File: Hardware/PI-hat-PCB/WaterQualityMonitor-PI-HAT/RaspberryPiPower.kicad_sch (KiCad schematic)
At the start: 27 parts

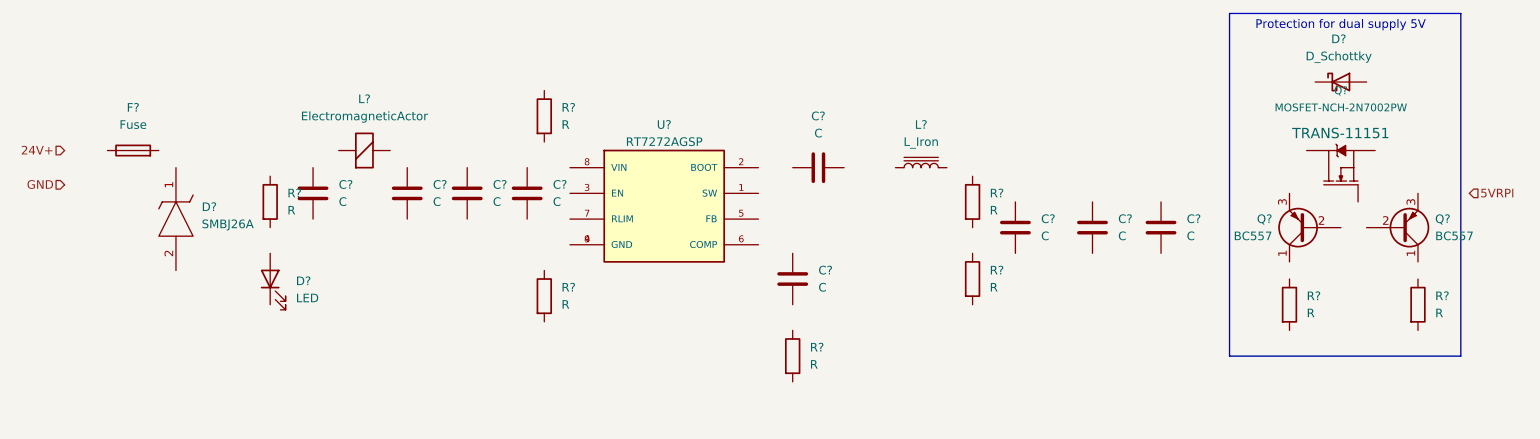
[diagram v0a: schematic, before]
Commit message: Finished powermanagementsystem
added RPI powersupply
added 5V and 3.3V power supply
changed some components (errors)
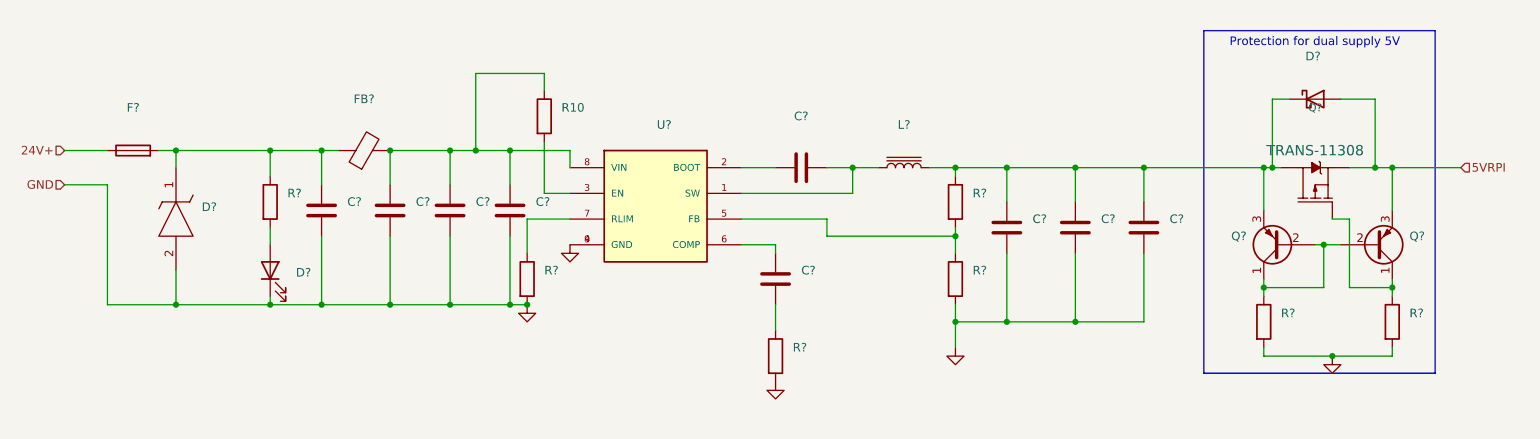
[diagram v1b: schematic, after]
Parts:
- removed C? (x4): C, symbol Device:C
- removed L?: ElectromagneticActor, symbol Device:ElectromagneticActor
- removed Q?: MOSFET-NCH-2N7002PW, SOT323, symbol SparkFun-DiscreteSemi:MOSFET-NCH-2N7002PW
- added C? (x4): (no value), symbol Device:C
- added FB?: (no value), symbol Device:FerriteBead
- added Q?: (no value), symbol SparkFun-DiscreteSemi:MOSFET_PCH-DMG2307L
- C? (x5): value C -> (none)
- D?: value D_Schottky -> (none)
- D?: value SMBJ26A -> (none); footprint DIOM5436X244N -> (none)
- D?: value LED -> (none)
- F?: value Fuse -> (none)
- L?: value L_Iron -> (none)
- Q? (x2): value BC557 -> (none); footprint Package_TO_SOT_THT:TO-92_Inline -> (none)
- R10: renamed from R?; value R -> (none)
- R? (x7): value R -> (none)
- U?: value RT7272AGSP -> (none); footprint SOIC127P599X175-9N -> (none)
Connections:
- net 24V+: now also F?.1
- net 5VRPI: now also D?.2 (A), Q?.3 (E), Q?.2 (S)
- net GND: now also C?.1, C?.1, C?.2, D?.1 (K), D?.2, R?.2, R?.2, R?.2, R?.2, R?.2, U?.4 (GND), U?.9 (GND), C?.1, C?.2, C?.2, C?.2
- net at R?.1: now also C?.1, D?.1, F?.2, FB?.1
- net at R?.2: now also D?.2 (A)
- net at R?.1: now also Q?.1 (C), Q?.1 (G)
- net at Q?.1 (C): now also Q?.2 (B), Q?.2 (B), R?.1
- net at Q?.3 (E): now also C?.2, C?.2, D?.1 (K), L?.2, R?.1, C?.2, Q?.3 (D)
- net at R10.1: now also U?.8 (VIN), C?.1, C?.1, C?.1, FB?.2
- net at R10.2: now also U?.3 (EN)
- net at R?.1: now also C?.1
- net at R?.1: now also U?.7 (RLIM)
- net at U?.1 (SW): now also C?.2, L?.1
- net at U?.2 (BOOT): now also C?.1
- net at U?.5 (FB): now also R?.1, R?.2
- net at U?.6 (COMP): now also C?.2
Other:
- moved on the sheet: C?, D?, L?, Q?, R?, U?

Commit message: started heating and cooling design
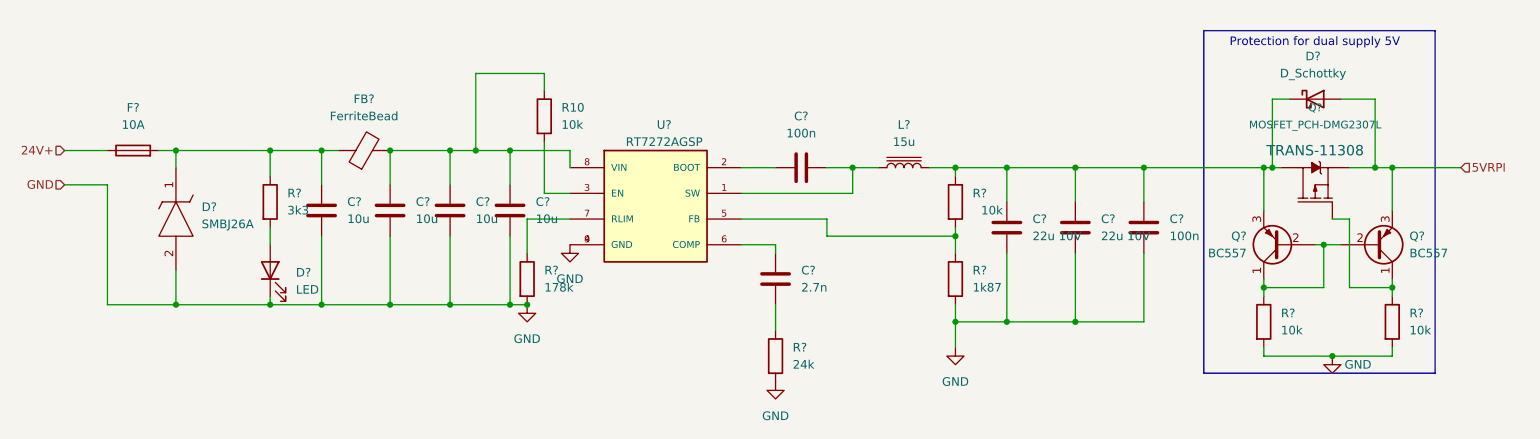
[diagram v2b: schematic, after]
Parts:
- C? (x4): value (none) -> 10u
- C? (x2): value (none) -> 22u 10V
- C? (x2): value (none) -> 100n
- C?: value (none) -> 2.7n
- D?: value (none) -> D_Schottky
- D?: value (none) -> SMBJ26A; footprint (none) -> DIOM5436X244N
- D?: value (none) -> LED
- F?: value (none) -> 10A
- FB?: value (none) -> FerriteBead
- L?: value (none) -> 15u
- Q?: value (none) -> MOSFET_PCH-DMG2307L; footprint (none) -> SOT23-3
- Q? (x2): value (none) -> BC557; footprint (none) -> Package_TO_SOT_THT:TO-92_Inline
- R10, R? (x3): value (none) -> 10k
- R?: value (none) -> 3k3
- R?: value (none) -> 24k
- R?: value (none) -> 178k
- R?: value (none) -> 1k87
- U?: value (none) -> RT7272AGSP; footprint (none) -> SOIC127P599X175-9N
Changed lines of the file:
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@@
       (effects (font (size 1.143 1.143)))
     )
-    (property "Value" "" (id 1) (at 232.41 87.63 90)
+    (property "Value" "MOSFET_PCH-DMG2307L" (id 1) (at 232.41 87.63 90)
       (effects (font (size 1.143 1.143)))
     )
-    (property "Footprint" "" (id 2) (at 226.06 96.52 0)
+    (property "Footprint" "SOT23-3" (id 2) (at 226.06 96.52 0)
       (effects (font (size 0.508 0.508)) hide)
     )
@@
       (effects (font (size 1.27 1.27)) (justify left))
     )
-    (property "Value" "" (id 1) (at 80.01 100.3299 0)
+    (property "Value" "3k3" (id 1) (at 80.01 100.3299 0)
       (effects (font (size 1.27 1.27)) (justify left))
     )
@@
       (effects (font (size 1.27 1.27)) (justify left))
     )
-    (property "Value" "" (id 1) (at 246.38 118.1099 0)
+    (property "Value" "10k" (id 1) (at 246.38 118.1099 0)
       (effects (font (size 1.27 1.27)) (justify left))
     )
@@
       (effects (font (size 1.27 1.27)) (justify left))
     )
-    (property "Value" "" (id 1) (at 222.25 106.6799 0)
-      (effects (font (size 1.27 1.27)) (justify left))
-    )
-    (property "Footprint" "" (id 2) (at 222.25 103.505 0)
+    (property "Value" "BC557" (id 1) (at 222.25 106.6799 0)
+      (effects (font (size 1.27 1.27)) (justify left))
+    )
+    (property "Footprint" "Package_TO_SOT_THT:TO-92_Inline" (id 2) (at 222.25 103.505 0)
       (effects (font (size 1.27 1.27) italic) (justify left) hide)
     )
@@
       (effects (font (size 1.27 1.27)) (justify left))
     )
-    (property "Value" "" (id 1) (at 120.65 87.6299 0)
+    (property "Value" "10k" (id 1) (at 120.65 87.6299 0)
       (effects (font (size 1.27 1.27)) (justify left))
     )
@@
       (effects (font (size 1.27 1.27)) (justify left))
     )
-    (property "Value" "" (id 1) (at 154.94 123.1899 0)
+    (property "Value" "24k" (id 1) (at 154.94 123.1899 0)
       (effects (font (size 1.27 1.27)) (justify left))
     )
@@
       (effects (font (size 1.27 1.27)) (justify left))
     )
-    (property "Value" "" (id 1) (at 118.11 111.7599 0)
+    (property "Value" "178k" (id 1) (at 118.11 111.7599 0)
       (effects (font (size 1.27 1.27)) (justify left))
     )
@@
       (effects (font (size 1.27 1.27)) (justify left))
     )
-    (property "Value" "" (id 1) (at 227.33 118.1099 0)
+    (property "Value" "10k" (id 1) (at 227.33 118.1099 0)
       (effects (font (size 1.27 1.27)) (justify left))
     )
@@
       (effects (font (size 1.27 1.27)) (justify left))
     )
-    (property "Value" "" (id 1) (at 88.9 101.5999 0)
+    (property "Value" "10u" (id 1) (at 88.9 101.5999 0)
       (effects (font (size 1.27 1.27)) (justify left))
     )
@@
       (effects (font (size 1.27 1.27)) (justify right))
     )
-    (property "Value" "" (id 1) (at 190.5 104.1399 0)
+    (property "Value" "22u 10V" (id 1) (at 190.5 104.1399 0)
       (effects (font (size 1.27 1.27)) (justify right))
     )
@@
       (effects (font (size 1.27 1.27)) (justify left))
     )
-    (property "Value" "" (id 1) (at 99.06 101.5999 0)
+    (property "Value" "10u" (id 1) (at 99.06 101.5999 0)
       (effects (font (size 1.27 1.27)) (justify left))
     )
@@
       (effects (font (size 1.27 1.27)) (justify left))
     )
-    (property "Value" "" (id 1) (at 246.38 106.6799 0)
-      (effects (font (size 1.27 1.27)) (justify left))
-    )
-    (property "Footprint" "" (id 2) (at 246.38 103.505 0)
+    (property "Value" "BC557" (id 1) (at 246.38 106.6799 0)
+      (effects (font (size 1.27 1.27)) (justify left))
+    )
+    (property "Footprint" "Package_TO_SOT_THT:TO-92_Inline" (id 2) (at 246.38 103.505 0)
       (effects (font (size 1.27 1.27) italic) (justify left) hide)
     )
@@
       (effects (font (size 1.27 1.27)) (justify right))
     )
-    (property "Value" "" (id 1) (at 210.82 104.1399 0)
+    (property "Value" "100n" (id 1) (at 210.82 104.1399 0)
       (effects (font (size 1.27 1.27)) (justify right))
     )
@@
       (effects (font (size 1.27 1.27)) (justify left))
     )
-    (property "Value" "" (id 1) (at 107.95 101.5999 0)
+    (property "Value" "10u" (id 1) (at 107.95 101.5999 0)
       (effects (font (size 1.27 1.27)) (justify left))
     )
@@
     (in_bom yes) (on_board yes) (fields_autoplaced)
     (property "Reference" "D?" (id 0) (at 232.0925 77.47 0))
-    (property "Value" "" (id 1) (at 232.0925 80.01 0))
+    (property "Value" "D_Schottky" (id 1) (at 232.0925 80.01 0))
     (property "Footprint" "" (id 2) (at 232.41 83.82 0)
       (effects (font (size 1.27 1.27)) hide)
@@
       (effects (font (size 1.27 1.27)) hide)
     )
-    (property "Value" "" (id 1) (at 238.76 123.19 0))
+    (property "Value" "GND" (id 1) (at 238.76 123.19 0))
     (property "Footprint" "" (id 2) (at 234.95 121.92 0)
       (effects (font (size 1.27 1.27)) hide)
@@
     (in_bom yes) (on_board yes) (fields_autoplaced)
     (property "Reference" "FB?" (id 0) (at 91.3892 83.82 90))
-    (property "Value" "" (id 1) (at 91.3892 86.36 90))
+    (property "Value" "FerriteBead" (id 1) (at 91.3892 86.36 90))
     (property "Footprint" "" (id 2) (at 91.44 93.218 90)
       (effects (font (size 1.27 1.27)) hide)
@@
       (effects (font (size 1.27 1.27)) (justify left))
     )
-    (property "Value" "" (id 1) (at 67.31 102.3619 90)
-      (effects (font (size 1.27 1.27)) (justify left))
-    )
-    (property "Footprint" "" (id 2) (at 67.31 104.14 0)
+    (property "Value" "SMBJ26A" (id 1) (at 67.31 102.3619 90)
+      (effects (font (size 1.27 1.27)) (justify left))
+    )
+    (property "Footprint" "DIOM5436X244N" (id 2) (at 67.31 104.14 0)
       (effects (font (size 1.27 1.27)) (justify left bottom) hide)
     )
@@
     (in_bom yes) (on_board yes) (fields_autoplaced)
     (property "Reference" "U?" (id 0) (at 135.89 87.63 0))
-    (property "Value" "" (id 1) (at 135.89 90.17 0))
-    (property "Footprint" "" (id 2) (at 127 110.49 0)
+    (property "Value" "RT7272AGSP" (id 1) (at 135.89 90.17 0))
+    (property "Footprint" "SOIC127P599X175-9N" (id 2) (at 127 110.49 0)
       (effects (font (size 1.27 1.27)) (justify left bottom) hide)
     )
@@
       (effects (font (size 1.27 1.27)) (justify right))
     )
-    (property "Value" "" (id 1) (at 81.28 112.0774 90)
+    (property "Value" "LED" (id 1) (at 81.28 112.0774 90)
       (effects (font (size 1.27 1.27)) (justify right))
     )
@@
       (effects (font (size 1.27 1.27)) hide)
     )
-    (property "Value" "" (id 1) (at 179.07 125.73 0))
+    (property "Value" "GND" (id 1) (at 179.07 125.73 0))
     (property "Footprint" "" (id 2) (at 179.07 120.65 0)
       (effects (font (size 1.27 1.27)) hide)
@@
       (effects (font (size 1.27 1.27)) hide)
     )
-    (property "Value" "" (id 1) (at 121.92 110.49 0))
+    (property "Value" "GND" (id 1) (at 121.92 110.49 0))
     (property "Footprint" "" (id 2) (at 121.92 105.41 0)
       (effects (font (size 1.27 1.27)) hide)
@@
       (effects (font (size 1.27 1.27)) (justify right))
     )
-    (property "Value" "" (id 1) (at 156.21 111.7599 0)
+    (property "Value" "2.7n" (id 1) (at 156.21 111.7599 0)
       (effects (font (size 1.27 1.27)) (justify right))
     )
@@
       (effects (font (size 1.27 1.27)) (justify right))
     )
-    (property "Value" "" (id 1) (at 200.66 104.1399 0)
+    (property "Value" "22u 10V" (id 1) (at 200.66 104.1399 0)
       (effects (font (size 1.27 1.27)) (justify right))
     )
@@
       (effects (font (size 1.27 1.27)) (justify left))
     )
-    (property "Value" "" (id 1) (at 182.88 100.3299 0)
+    (property "Value" "10k" (id 1) (at 182.88 100.3299 0)
       (effects (font (size 1.27 1.27)) (justify left))
     )
@@
       (effects (font (size 1.27 1.27)) (justify left))
     )
-    (property "Value" "" (id 1) (at 181.61 111.7599 0)
+    (property "Value" "1k87" (id 1) (at 181.61 111.7599 0)
       (effects (font (size 1.27 1.27)) (justify left))
     )
@@
       (effects (font (size 1.27 1.27)) hide)
     )
-    (property "Value" "" (id 1) (at 152.4 130.81 0))
+    (property "Value" "GND" (id 1) (at 152.4 130.81 0))
     (property "Footprint" "" (id 2) (at 152.4 125.73 0)
       (effects (font (size 1.27 1.27)) hide)
@@
     (in_bom yes) (on_board yes) (fields_autoplaced)
     (property "Reference" "C?" (id 0) (at 156.21 86.36 90))
-    (property "Value" "" (id 1) (at 156.21 88.9 90))
+    (property "Value" "100n" (id 1) (at 156.21 88.9 90))
     (property "Footprint" "" (id 2) (at 160.02 93.0148 0)
       (effects (font (size 1.27 1.27)) hide)
@@
       (effects (font (size 1.27 1.27)) (justify left))
     )
-    (property "Value" "" (id 1) (at 116.84 101.5999 0)
+    (property "Value" "10u" (id 1) (at 116.84 101.5999 0)
       (effects (font (size 1.27 1.27)) (justify left))
     )
@@
     (in_bom yes) (on_board yes) (fields_autoplaced)
     (property "Reference" "L?" (id 0) (at 171.45 87.63 90))
-    (property "Value" "" (id 1) (at 171.45 90.17 90))
+    (property "Value" "15u" (id 1) (at 171.45 90.17 90))
     (property "Footprint" "" (id 2) (at 171.45 93.98 0)
       (effects (font (size 1.27 1.27)) hide)
@@
       (effects (font (size 1.27 1.27)) hide)
     )
-    (property "Value" "" (id 1) (at 115.57 119.38 0))
+    (property "Value" "GND" (id 1) (at 115.57 119.38 0))
     (property "Footprint" "" (id 2) (at 115.57 114.3 0)
       (effects (font (size 1.27 1.27)) hide)
@@
     (in_bom yes) (on_board yes) (fields_autoplaced)
     (property "Reference" "F?" (id 0) (at 57.15 85.09 90))
-    (property "Value" "" (id 1) (at 57.15 87.63 90))
+    (property "Value" "10A" (id 1) (at 57.15 87.63 90))
     (property "Footprint" "" (id 2) (at 57.15 93.218 90)
       (effects (font (size 1.27 1.27)) hide)

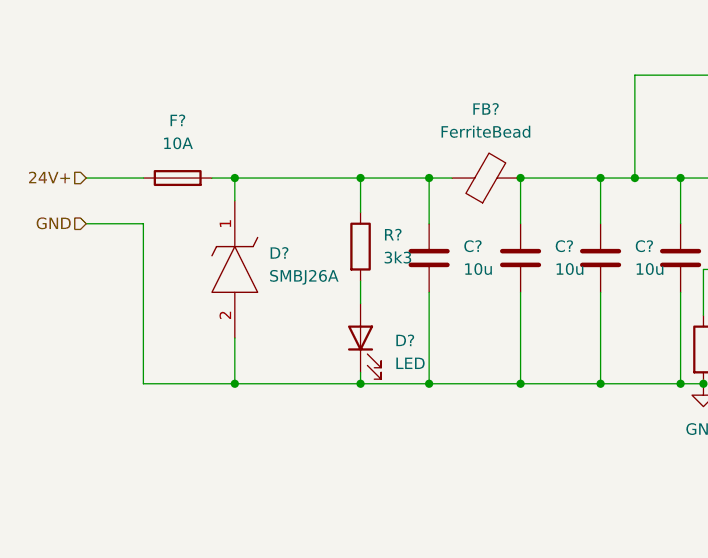
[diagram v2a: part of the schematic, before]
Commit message: Enhanced schematics
Moved protection circuits to main schematic
changed tmc2208 VIO to 3.3V (5V is also fine)
added fuses to heat and cooling schematic
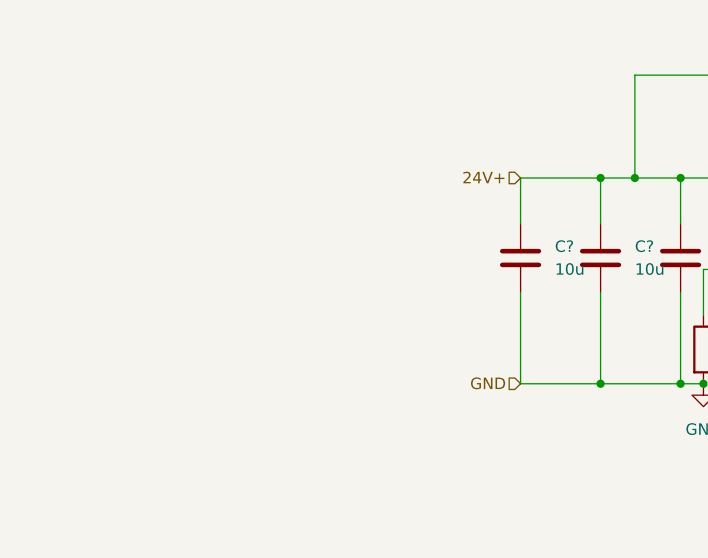
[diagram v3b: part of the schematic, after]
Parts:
- removed C?: 10u, symbol Device:C
- removed D?: SMBJ26A, DIOM5436X244N, symbol SamacSys_Parts:SMBJ26A
- removed D?: LED, symbol Device:LED
- removed F?: 10A, symbol Device:Fuse
- removed FB?: FerriteBead, symbol Device:FerriteBead
- removed R?: 3k3, symbol Device:R
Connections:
- net 24V+: now also C?.1, C?.1, C?.1, R10.1, U?.8 (VIN)

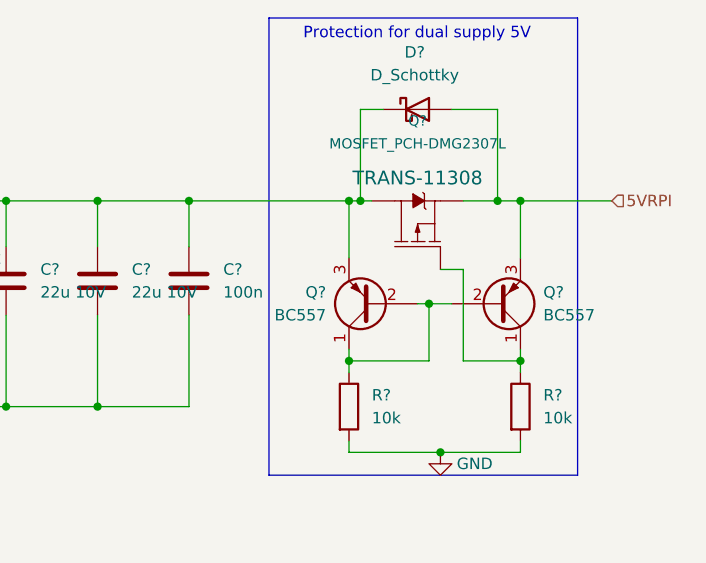
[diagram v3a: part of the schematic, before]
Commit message: updated power management circuit
also added extra notes to  conversation 6.
added datasheet.
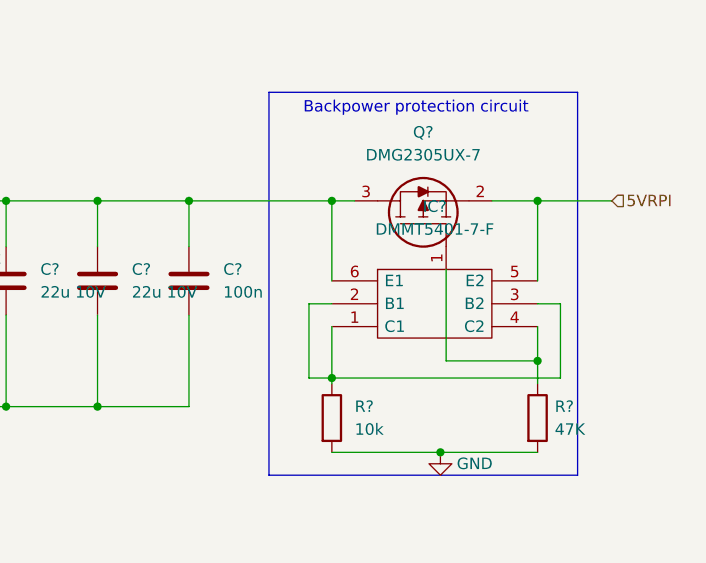
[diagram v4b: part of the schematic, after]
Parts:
- removed D?: D_Schottky, symbol Device:D_Schottky
- removed Q?: MOSFET_PCH-DMG2307L, SOT23-3, symbol SparkFun-DiscreteSemi:MOSFET_PCH-DMG2307L
- removed Q? (x2): BC557, Package_TO_SOT_THT:TO-92_Inline, symbol Transistor_BJT:BC557
- added IC?: DMMT5401-7-F, SOT95P285X140-6N, symbol SamacSys_Parts:DMMT5401-7-F
- added Q?: DMG2305UX-7, SOT96P240X110-3N, symbol SamacSys_Parts:DMG2305UX-7
- R?: value 10k -> 47K
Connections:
- net 5VRPI: now also IC?.5 (E2), Q?.2
- net at R?.1: now also IC?.4 (C2), Q?.1
- net at C?.2, C?.2, C?.2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: now also IC?.6 (E1), Q?.3
- net at R?.1: now also IC?.1 (C1), IC?.2 (B1), IC?.3 (B2)
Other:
- note added: "Backpower protection circuit"
- note removed: "Protection for dual supply 5V"
- moved on the sheet: R?

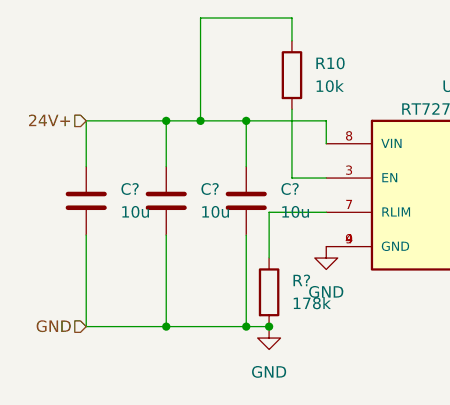
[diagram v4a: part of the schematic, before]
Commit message: changed PSU voltage from 24V to 12V
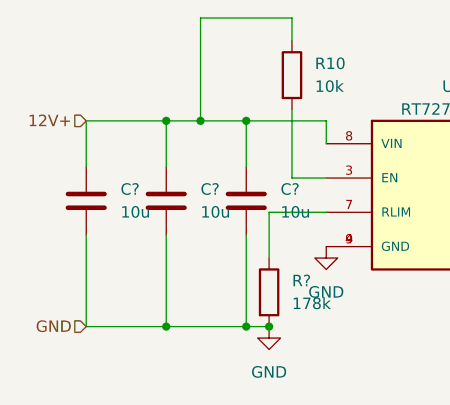
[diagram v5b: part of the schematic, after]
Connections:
- net 24V+ renamed 12V+
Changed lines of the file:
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@@
     (effects (font (size 1.27 1.27)) (justify left))
   )
-  (hierarchical_label "24V+" (shape input) (at 95.25 91.44 180)
+  (hierarchical_label "12V+" (shape input) (at 95.25 91.44 180)
     (effects (font (size 1.27 1.27)) (justify right))
   )
